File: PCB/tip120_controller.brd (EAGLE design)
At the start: 52.4 x 37.5 mm, 10 parts, among them J1 AUDIO_JACK_3.5MM_PTH, Q1 TIP120, X1 12V

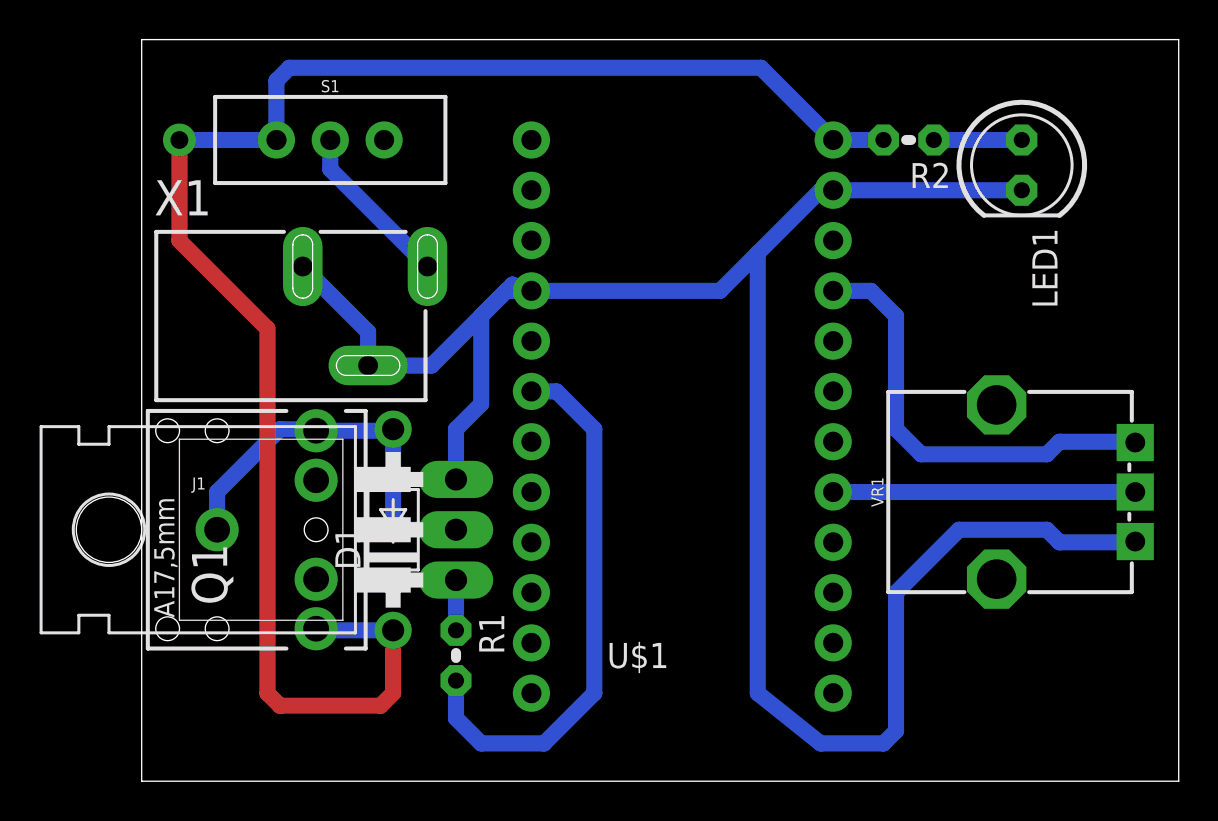
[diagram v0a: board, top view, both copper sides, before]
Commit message: added ground plane, moved led
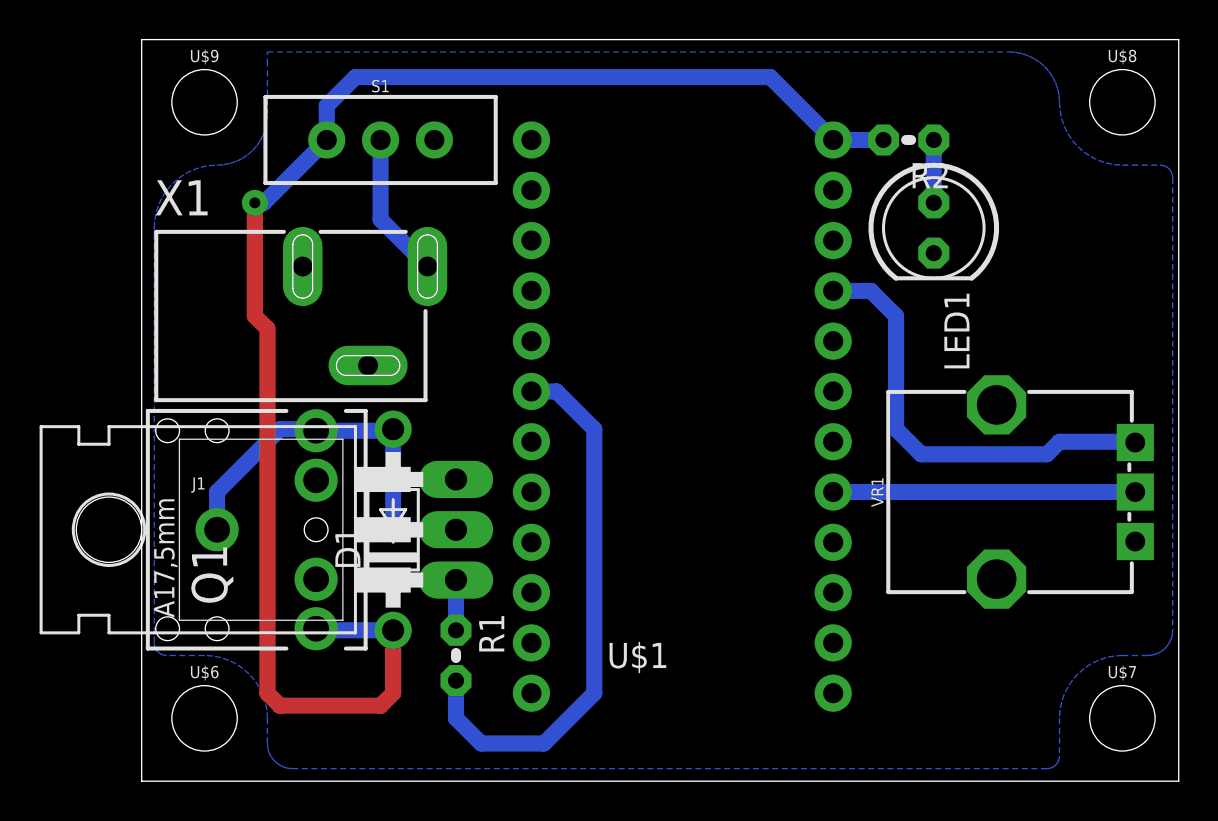
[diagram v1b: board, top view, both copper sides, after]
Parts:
- added U$6, U$7, U$8, U$9: (no value), SparkFun-Hardware:STAND-OFF
- moved LED1 5.46 mm to (39.4, 74.3)
- moved S1 2.54 mm to (11.4, 78.7)
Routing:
- net AGND: track 106.2 -> 0.00 mm
- net N$8: track 84.1 -> 75.7 mm
- net N$3: track 4.45 -> 3.17 mm
- net N$7: track 8.42 -> 7.37 mm
- added copper zone on layer 16, net AGND
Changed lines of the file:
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@@
 <?xml version="1.0" encoding="utf-8"?>
 <!DOCTYPE eagle SYSTEM "eagle.dtd">
-<eagle version="8.7.1">
+<eagle version="9.0.0">
 <drawing>
 <settings>
@@
 <setting verticaltext="up"/>
 </settings>
-<grid distance="0.025" unitdist="inch" unit="inch" style="lines" multiple="1" display="no" altdistance="0.025" altunitdist="inch" altunit="inch"/>
+<grid distance="0.025" unitdist="inch" unit="mm" style="lines" multiple="1" display="yes" altdistance="0.025" altunitdist="inch" altunit="mm"/>
 <layers>
 <layer number="1" name="Top" color="4" fill="1" visible="yes" active="yes"/>
@@
 <attribute name="OC_NEWARK" value="unknown" x="0" y="69.85" size="1.778" layer="27" rot="R270" display="off"/>
 </element>
-<element name="S1" library="SparkFun-Switches" package="SWITCH_SPDT_PTH_11.6X4.0MM_KIT" value="12V" x="8.89" y="78.74" rot="R270">
-<attribute name="PROD_ID" value="SWCH-08261" x="8.89" y="78.74" size="1.778" layer="27" rot="R270" display="off"/>
-<attribute name="SF_SKU" value="COM-00102" x="8.89" y="78.74" size="1.778" layer="27" rot="R270" display="off"/>
+<element name="S1" library="SparkFun-Switches" package="SWITCH_SPDT_PTH_11.6X4.0MM_KIT" value="12V" x="11.43" y="78.74" rot="R270">
+<attribute name="PROD_ID" value="SWCH-08261" x="11.43" y="78.74" size="1.778" layer="27" rot="R270" display="off"/>
+<attribute name="SF_SKU" value="COM-00102" x="11.43" y="78.74" size="1.778" layer="27" rot="R270" display="off"/>
 </element>
 <element name="R2" library="resistor" library_urn="urn:adsk.eagle:library:348" package="0204V" package3d_urn="urn:adsk.eagle:package:25948/1" value="220" x="38.1" y="78.74" rot="R180"/>
-<element name="LED1" library="led" library_urn="urn:adsk.eagle:library:259" package="LED5MM" package3d_urn="urn:adsk.eagle:package:15799/2" value="RED" x="43.815" y="77.47" rot="R270"/>
+<element name="LED1" library="led" library_urn="urn:adsk.eagle:library:259" package="LED5MM" package3d_urn="urn:adsk.eagle:package:15799/2" value="RED" x="39.37" y="74.295" rot="R270"/>
 <element name="Q1" library="transistor-power" library_urn="urn:adsk.eagle:library:400" package="TO220AH" package3d_urn="urn:adsk.eagle:package:29488/1" value="TIP120" x="8.89" y="59.055" rot="R90"/>
 <element name="R1" library="resistor" library_urn="urn:adsk.eagle:library:348" package="0204V" package3d_urn="urn:adsk.eagle:package:25948/1" value="2.2k" x="15.24" y="52.705" rot="R270"/>
@@
 </element>
 <element name="D1" library="diode" library_urn="urn:adsk.eagle:library:210" package="DO41-10" package3d_urn="urn:adsk.eagle:package:43336/1" value="1N4004" x="12.065" y="59.055" rot="R90"/>
+<element name="U$6" library="SparkFun-Hardware" package="STAND-OFF" value="" x="2.54" y="49.53"/>
+<element name="U$7" library="SparkFun-Hardware" package="STAND-OFF" value="" x="48.895" y="49.53"/>
+<element name="U$8" library="SparkFun-Hardware" package="STAND-OFF" value="" x="48.895" y="80.645"/>
+<element name="U$9" library="SparkFun-Hardware" package="STAND-OFF" value="" x="2.54" y="80.645"/>
 </elements>
 <signals>
@@
 <contactref element="X1" pad="3"/>
 <contactref element="X1" pad="2"/>
-<wire x1="7.5" y1="72.35" x2="10.8" y2="69.05" width="0.8128" layer="16"/>
-<wire x1="10.8" y1="69.05" x2="10.8" y2="67.35" width="0.8128" layer="16"/>
-<wire x1="43.815" y1="76.2" x2="34.29" y2="76.2" width="0.8128" layer="16"/>
-<wire x1="10.8" y1="67.35" x2="14.01" y2="67.35" width="0.8128" layer="16"/>
-<wire x1="18.415" y1="71.12" x2="18.0975" y2="71.4375" width="0.8128" layer="16"/>
 <contactref element="Q1" pad="E"/>
-<wire x1="16.51" y1="65.405" x2="16.51" y2="69.85" width="0.8128" layer="16"/>
 <contactref element="U$1" pad="4"/>
-<wire x1="19.05" y1="71.12" x2="18.415" y2="71.12" width="0.8128" layer="16"/>
-<wire x1="16.51" y1="69.85" x2="17.78" y2="71.12" width="0.8128" layer="16"/>
-<wire x1="17.78" y1="71.12" x2="19.05" y2="71.12" width="0.8128" layer="16"/>
-<wire x1="14.01" y1="67.35" x2="18.0975" y2="71.4375" width="0.8128" layer="16"/>
 <contactref element="VR1" pad="P$1"/>
-<wire x1="30.48" y1="73.025" x2="30.48" y2="50.8" width="0.8128" layer="16"/>
-<wire x1="30.48" y1="50.8" x2="33.655" y2="48.26" width="0.8128" layer="16"/>
-<wire x1="33.655" y1="48.26" x2="36.83" y2="48.26" width="0.8128" layer="16"/>
-<wire x1="36.83" y1="48.26" x2="37.465" y2="48.895" width="0.8128" layer="16"/>
-<wire x1="37.465" y1="48.895" x2="37.465" y2="55.88" width="0.8128" layer="16"/>
-<wire x1="37.465" y1="55.88" x2="40.64" y2="59.055" width="0.8128" layer="16"/>
-<wire x1="40.64" y1="59.055" x2="45.085" y2="59.055" width="0.8128" layer="16"/>
-<wire x1="45.085" y1="59.055" x2="45.72" y2="58.42" width="0.8128" layer="16"/>
-<wire x1="45.72" y1="58.42" x2="49.505" y2="58.42" width="0.8128" layer="16"/>
-<wire x1="49.505" y1="58.42" x2="49.545" y2="58.46" width="0.8128" layer="16"/>
-<wire x1="15.24" y1="64.135" x2="16.51" y2="65.405" width="0.8128" layer="16"/>
-<wire x1="15.24" y1="61.595" x2="15.24" y2="64.135" width="0.8128" layer="16"/>
-<wire x1="19.05" y1="71.12" x2="28.575" y2="71.12" width="0.8128" layer="16"/>
-<wire x1="28.575" y1="71.12" x2="30.48" y2="73.025" width="0.8128" layer="16"/>
-<wire x1="30.48" y1="73.025" x2="33.655" y2="76.2" width="0.8128" layer="16"/>
-<wire x1="33.655" y1="76.2" x2="34.29" y2="76.2" width="0.8128" layer="16"/>
+<polygon width="0.254" layer="16" isolate="0.8128">
+<vertex x="5.715" y="83.185"/>
+<vertex x="43.18" y="83.185" curve="-90"/>
+<vertex x="45.72" y="80.645" curve="90"/>
+<vertex x="48.895" y="77.47"/>
+<vertex x="50.8" y="77.47" curve="-90"/>
+<vertex x="51.435" y="76.835"/>
+<vertex x="51.435" y="53.975" curve="-90"/>
+<vertex x="50.165" y="52.705"/>
+<vertex x="48.895" y="52.705" curve="90"/>
+<vertex x="45.72" y="49.53"/>
+<vertex x="45.72" y="47.625" curve="-90"/>
+<vertex x="45.085" y="46.99"/>
+<vertex x="6.985" y="46.99" curve="-90"/>
+<vertex x="5.715" y="48.26"/>
+<vertex x="5.715" y="49.53" curve="90"/>
+<vertex x="2.54" y="52.705"/>
+<vertex x="0.635" y="52.705" curve="-90"/>
+<vertex x="0" y="53.34"/>
+<vertex x="0" y="74.295" curve="-90"/>
+<vertex x="3.175" y="77.47" curve="90"/>
+<vertex x="5.715" y="80.01"/>
+<vertex x="5.715" y="82.55"/>
+</polygon>
 </signal>
 <signal name="N$3">
 <contactref element="LED1" pad="A"/>
 <contactref element="R2" pad="1"/>
-<wire x1="39.37" y1="78.74" x2="43.815" y2="78.74" width="0.8128" layer="16"/>
+<wire x1="39.37" y1="78.74" x2="39.37" y2="75.565" width="0.8128" layer="16"/>
 </signal>
 <signal name="N$7">
 <contactref element="X1" pad="1"/>
 <contactref element="S1" pad="2"/>
-<wire x1="13.8" y1="72.35" x2="8.89" y2="77.26" width="0.8128" layer="16"/>
-<wire x1="8.89" y1="77.26" x2="8.89" y2="78.74" width="0.8128" layer="16"/>
+<wire x1="13.8" y1="72.35" x2="11.43" y2="74.72" width="0.8128" layer="16"/>
+<wire x1="11.43" y1="74.72" x2="11.43" y2="78.74" width="0.8128" layer="16"/>
 </signal>
 <signal name="N$2">
@@
 <contactref element="U$1" pad="24"/>
 <wire x1="34.29" y1="78.74" x2="36.83" y2="78.74" width="0.8128" layer="16"/>
-<wire x1="30.6424" y1="82.3876" x2="34.29" y2="78.74" width="0.8128" layer="16"/>
-<wire x1="6.1722" y1="78.74" x2="6.1722" y2="81.7372" width="0.8128" layer="16"/>
-<wire x1="6.1722" y1="81.7372" x2="6.8226" y2="82.3876" width="0.8128" layer="16"/>
-<wire x1="6.8226" y1="82.3876" x2="30.6424" y2="82.3876" width="0.8128" layer="16"/>
-<wire x1="6.1722" y1="78.74" x2="1.27" y2="78.74" width="0.8128" layer="16"/>
-<via x="1.27" y="78.74" extent="1-16" drill="0.9"/>
-<wire x1="1.27" y1="78.74" x2="1.27" y2="73.66" width="0.8128" layer="1"/>
-<wire x1="1.27" y1="73.66" x2="5.715" y2="69.215" width="0.8128" layer="1"/>
 <wire x1="5.715" y1="50.8" x2="6.35" y2="50.165" width="0.8128" layer="1"/>
-<wire x1="5.715" y1="69.215" x2="5.715" y2="50.8" width="0.8128" layer="1"/>
+<wire x1="5.715" y1="50.8" x2="5.715" y2="69.215" width="0.8128" layer="1"/>
 <wire x1="6.35" y1="50.165" x2="11.43" y2="50.165" width="0.8128" layer="1"/>
 <wire x1="11.43" y1="50.165" x2="12.065" y2="50.8" width="0.8128" layer="1"/>
@@
 <wire x1="8.255" y1="53.975" x2="12.065" y2="53.975" width="0.8128" layer="16"/>
 <wire x1="12.065" y1="50.8" x2="12.065" y2="53.975" width="0.8128" layer="1"/>
+<wire x1="8.7122" y1="78.74" x2="8.7122" y2="80.4672" width="0.8128" layer="16"/>
+<wire x1="8.7122" y1="80.4672" x2="10.16" y2="81.915" width="0.8128" layer="16"/>
+<wire x1="10.16" y1="81.915" x2="31.115" y2="81.915" width="0.8128" layer="16"/>
+<wire x1="31.115" y1="81.915" x2="34.29" y2="78.74" width="0.8128" layer="16"/>
+<wire x1="5.715" y1="69.215" x2="5.08" y2="69.85" width="0.8128" layer="1"/>
+<wire x1="5.08" y1="69.85" x2="5.08" y2="75.565" width="0.8128" layer="1"/>
+<via x="5.08" y="75.565" extent="1-16" drill="0.55" diameter="0.35"/>
+<wire x1="5.08" y1="75.565" x2="5.5372" y2="75.565" width="0.8128" layer="16"/>
+<wire x1="5.5372" y1="75.565" x2="8.7122" y2="78.74" width="0.8128" layer="16"/>
 </signal>
 <signal name="N$1">

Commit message: adjust
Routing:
- net N$8: track 75.7 -> 73.2 mm
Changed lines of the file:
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@@
 <attribute name="SF_SKU" value="COM-09288" x="42.545" y="60.96" size="1.778" layer="27" display="off"/>
 </element>
-<element name="D1" library="diode" library_urn="urn:adsk.eagle:library:210" package="DO41-10" package3d_urn="urn:adsk.eagle:package:43336/1" value="1N4004" x="12.065" y="59.055" rot="R90"/>
+<element name="D1" library="diode" library_urn="urn:adsk.eagle:library:210" package="DO41-10" package3d_urn="urn:adsk.eagle:package:43336/1" value="1N4004" x="12.065" y="59.055" smashed="yes" rot="R90">
+<attribute name="NAME" x="10.414" y="57.023" size="1.27" layer="25" ratio="10" rot="R90"/>
+<attribute name="VALUE" x="14.859" y="57.023" size="1.27" layer="27" ratio="10" rot="R90"/>
+</element>
 <element name="U$6" library="SparkFun-Hardware" package="STAND-OFF" value="" x="2.54" y="49.53"/>
 <element name="U$7" library="SparkFun-Hardware" package="STAND-OFF" value="" x="48.895" y="49.53"/>
@@
 <contactref element="U$1" pad="24"/>
 <wire x1="34.29" y1="78.74" x2="36.83" y2="78.74" width="0.8128" layer="16"/>
-<wire x1="5.715" y1="50.8" x2="6.35" y2="50.165" width="0.8128" layer="1"/>
-<wire x1="5.715" y1="50.8" x2="5.715" y2="69.215" width="0.8128" layer="1"/>
-<wire x1="6.35" y1="50.165" x2="11.43" y2="50.165" width="0.8128" layer="1"/>
-<wire x1="11.43" y1="50.165" x2="12.065" y2="50.8" width="0.8128" layer="1"/>
 <contactref element="J1" pad="TIP"/>
 <contactref element="D1" pad="C"/>
 <wire x1="8.175" y1="54.055" x2="8.255" y2="53.975" width="0.8128" layer="16"/>
 <wire x1="8.255" y1="53.975" x2="12.065" y2="53.975" width="0.8128" layer="16"/>
-<wire x1="12.065" y1="50.8" x2="12.065" y2="53.975" width="0.8128" layer="1"/>
 <wire x1="8.7122" y1="78.74" x2="8.7122" y2="80.4672" width="0.8128" layer="16"/>
 <wire x1="8.7122" y1="80.4672" x2="10.16" y2="81.915" width="0.8128" layer="16"/>
 <wire x1="10.16" y1="81.915" x2="31.115" y2="81.915" width="0.8128" layer="16"/>
 <wire x1="31.115" y1="81.915" x2="34.29" y2="78.74" width="0.8128" layer="16"/>
-<wire x1="5.715" y1="69.215" x2="5.08" y2="69.85" width="0.8128" layer="1"/>
+<wire x1="5.08" y1="69.85" x2="5.715" y2="69.215" width="0.8128" layer="1"/>
 <wire x1="5.08" y1="69.85" x2="5.08" y2="75.565" width="0.8128" layer="1"/>
 <via x="5.08" y="75.565" extent="1-16" drill="0.55" diameter="0.35"/>
 <wire x1="5.08" y1="75.565" x2="5.5372" y2="75.565" width="0.8128" layer="16"/>
 <wire x1="5.5372" y1="75.565" x2="8.7122" y2="78.74" width="0.8128" layer="16"/>
+<wire x1="5.715" y1="69.215" x2="5.715" y2="52.07" width="0.8128" layer="1"/>
+<wire x1="5.715" y1="52.07" x2="6.35" y2="51.435" width="0.8128" layer="1"/>
+<wire x1="6.35" y1="51.435" x2="11.43" y2="51.435" width="0.8128" layer="1"/>
+<wire x1="11.43" y1="51.435" x2="12.065" y2="52.07" width="0.8128" layer="1"/>
+<wire x1="12.065" y1="52.07" x2="12.065" y2="53.975" width="0.8128" layer="1"/>
 </signal>
 <signal name="N$1">

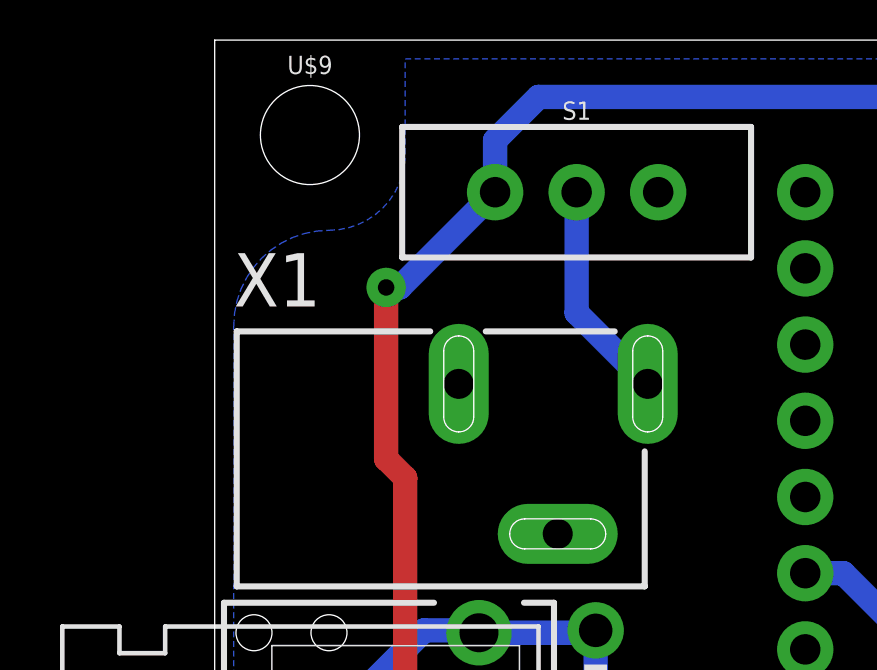
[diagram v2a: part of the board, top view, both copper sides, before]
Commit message: moved via so its not under dc jack, layout is done
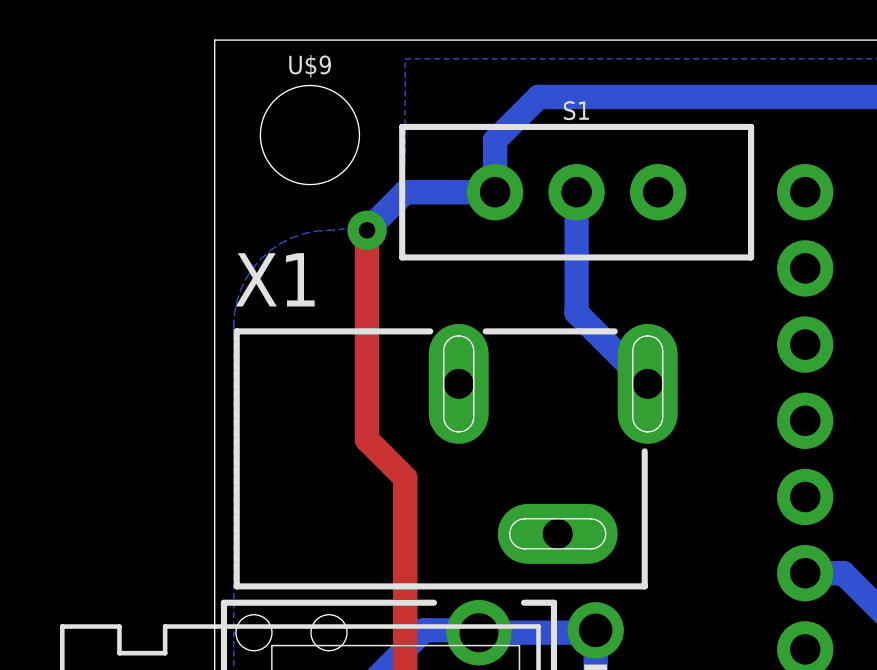
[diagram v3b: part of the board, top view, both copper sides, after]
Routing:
- net N$8: track 73.2 -> 75.2 mm
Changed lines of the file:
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@@
 <wire x1="10.16" y1="81.915" x2="31.115" y2="81.915" width="0.8128" layer="16"/>
 <wire x1="31.115" y1="81.915" x2="34.29" y2="78.74" width="0.8128" layer="16"/>
-<wire x1="5.08" y1="69.85" x2="5.715" y2="69.215" width="0.8128" layer="1"/>
-<wire x1="5.08" y1="69.85" x2="5.08" y2="75.565" width="0.8128" layer="1"/>
-<via x="5.08" y="75.565" extent="1-16" drill="0.55" diameter="0.35"/>
-<wire x1="5.08" y1="75.565" x2="5.5372" y2="75.565" width="0.8128" layer="16"/>
-<wire x1="5.5372" y1="75.565" x2="8.7122" y2="78.74" width="0.8128" layer="16"/>
+<via x="4.445" y="77.47" extent="1-16" drill="0.55" diameter="0.35"/>
 <wire x1="5.715" y1="69.215" x2="5.715" y2="52.07" width="0.8128" layer="1"/>
 <wire x1="5.715" y1="52.07" x2="6.35" y2="51.435" width="0.8128" layer="1"/>
@@
 <wire x1="11.43" y1="51.435" x2="12.065" y2="52.07" width="0.8128" layer="1"/>
 <wire x1="12.065" y1="52.07" x2="12.065" y2="53.975" width="0.8128" layer="1"/>
+<wire x1="5.715" y1="69.215" x2="4.445" y2="70.485" width="0.8128" layer="1"/>
+<wire x1="4.445" y1="70.485" x2="4.445" y2="77.47" width="0.8128" layer="1"/>
+<wire x1="4.445" y1="77.47" x2="5.715" y2="78.74" width="0.8128" layer="16"/>
+<wire x1="5.715" y1="78.74" x2="8.7122" y2="78.74" width="0.8128" layer="16"/>
 </signal>
 <signal name="N$1">

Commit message: silkscreen update
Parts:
- LED1: value RED -> (none)
- PJ-102A, S1: value 12V -> 6-12V
- renumbered X1 to PJ-102A
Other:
- board text added: "tip120 controller v3 summer 2018 caseyanderson.com awavepress.com"
